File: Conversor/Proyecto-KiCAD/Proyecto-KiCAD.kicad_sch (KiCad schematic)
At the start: 50 parts

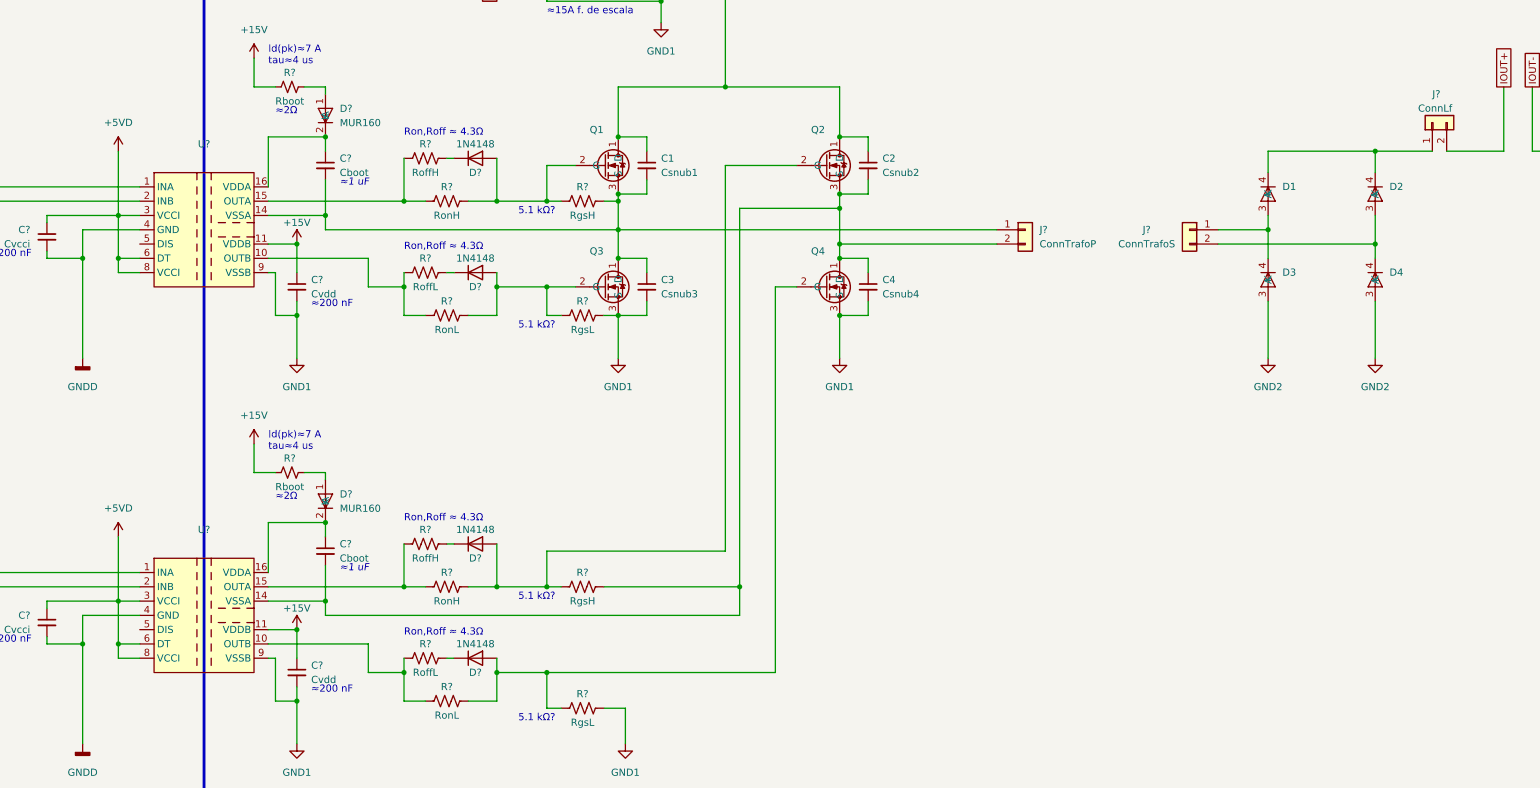
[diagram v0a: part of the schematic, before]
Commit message: Completar las fuentes aisladas del lado digital
- Falta hacer las fuentes del lado de potencia (sin las TRACO).
  - Se tiene que tomar la entrada de 12V-18V y pasarla por un regulador de 15V.
  - Despues esa salida de 15V se pasa por un regulador que la baje a 5V.
- Agregadas datasheets y notas:
  - Datasheets de regulador LM1117 para pasar de 5V a 3.3V para alimentar el DSP.
  - Notas de aplicacion de la fuente TRACO y explicaciones de corrientes sink y source.
- Hay que ver las cosas que me tiene que pasar Jorge de la alimentacion del DSP.
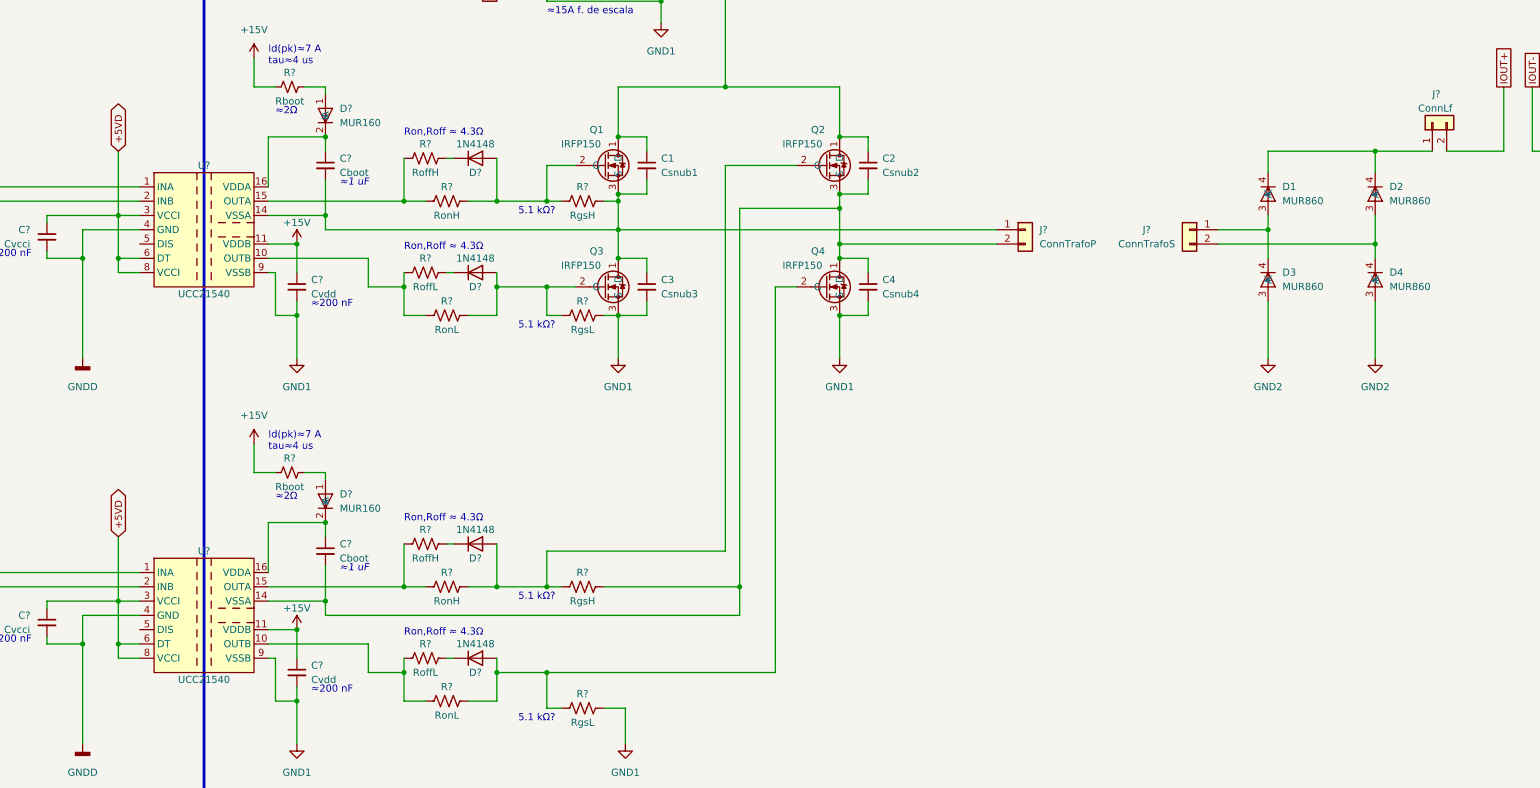
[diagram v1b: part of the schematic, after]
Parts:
- D1, D2, D3, D4: value (none) -> MUR860; footprint (none) -> Package_TO_SOT_THT:TO-220F-2_Vertical
- Q1, Q2, Q3, Q4: value (none) -> IRFP150; footprint (none) -> Package_TO_SOT_THT:TO-247-3_Vertical
- U? (x2): value (none) -> UCC21540; footprint (none) -> Package_SO:SOIC-16W_7.5x10.3mm_P1.27mm

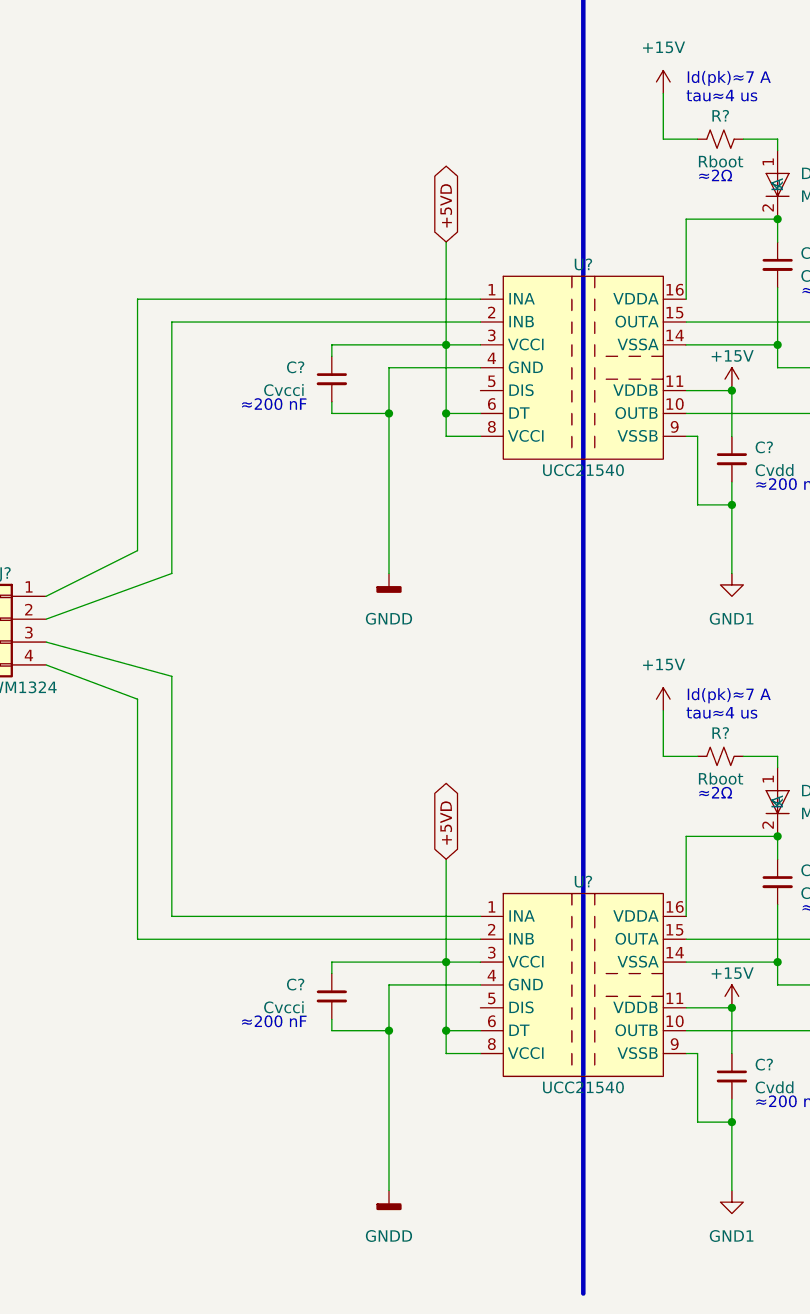
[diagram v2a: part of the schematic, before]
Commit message: Modificar las fuentes de alimentacion
- Falta la fuente regulada de 15V para Vdd de los drivers (Sale a partir de alimentacion de 24V?)
- El DSP se alimenta por +5V a traves de la placa de prueba
- 3.3V para la proteccion a la salida del AO del ACS709
- Agregada datasheet del regulador MC7805 de 12-18V a 5VP
- Uso el pin de dead-time (DT) de los drivers para evitar corto en una pata del
  puente de MOSFETs (200ns de dead-time)
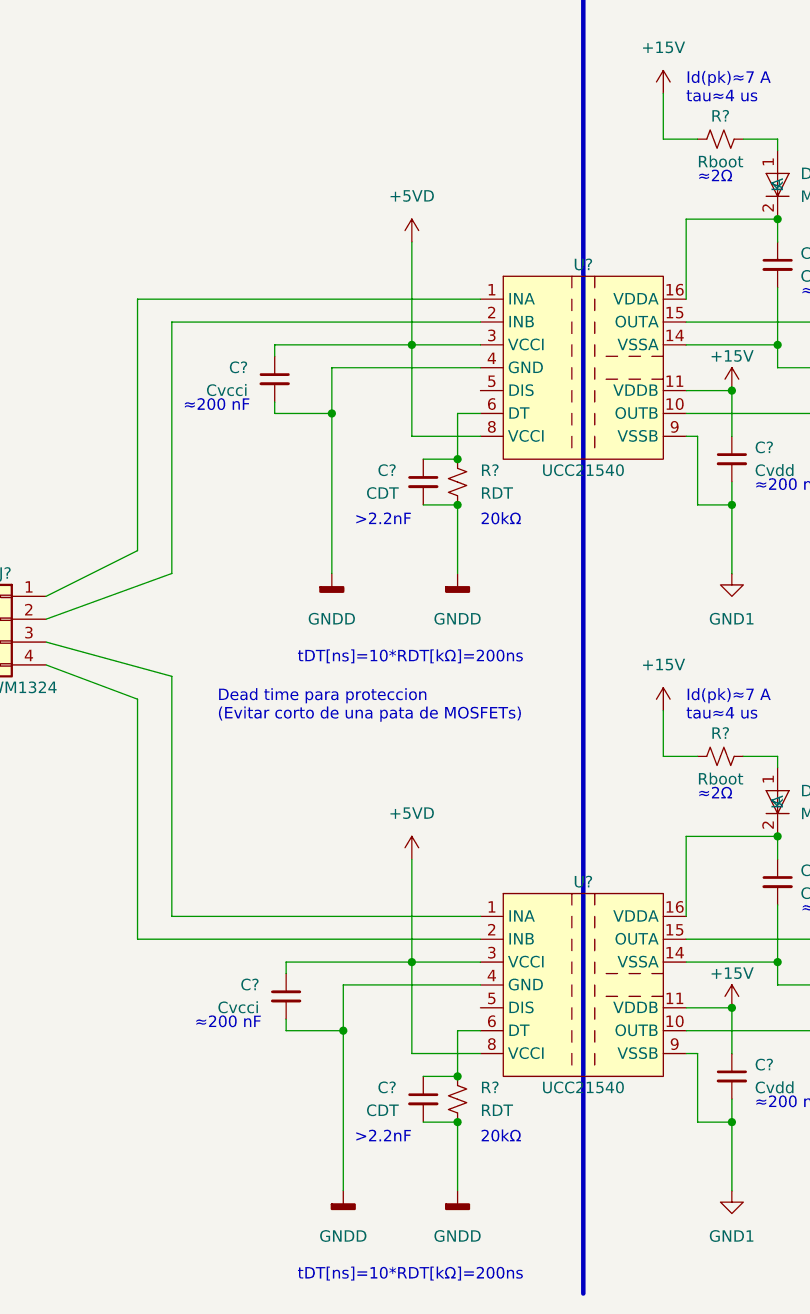
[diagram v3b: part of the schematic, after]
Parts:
- added C? (x2): CDT, symbol Device:C_Small
- added R? (x2): RDT, symbol Device:R_Small_US
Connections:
- net +5VD: no longer U?.6 (DT), U?.6 (DT)
- net GNDD: now also C?.2, C?.2, R?.2, R?.2
- new net: C?.1, R?.1, U?.6 (DT) (x2)
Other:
- note added: "20kΩ"
- note added: ">2.2nF"
- note added: "Dead time para proteccion (Evitar corto de una pata de MOSFETs)"
- note added: "tDT[ns]=10*RDT[kΩ]=200ns"
- moved on the sheet: C?

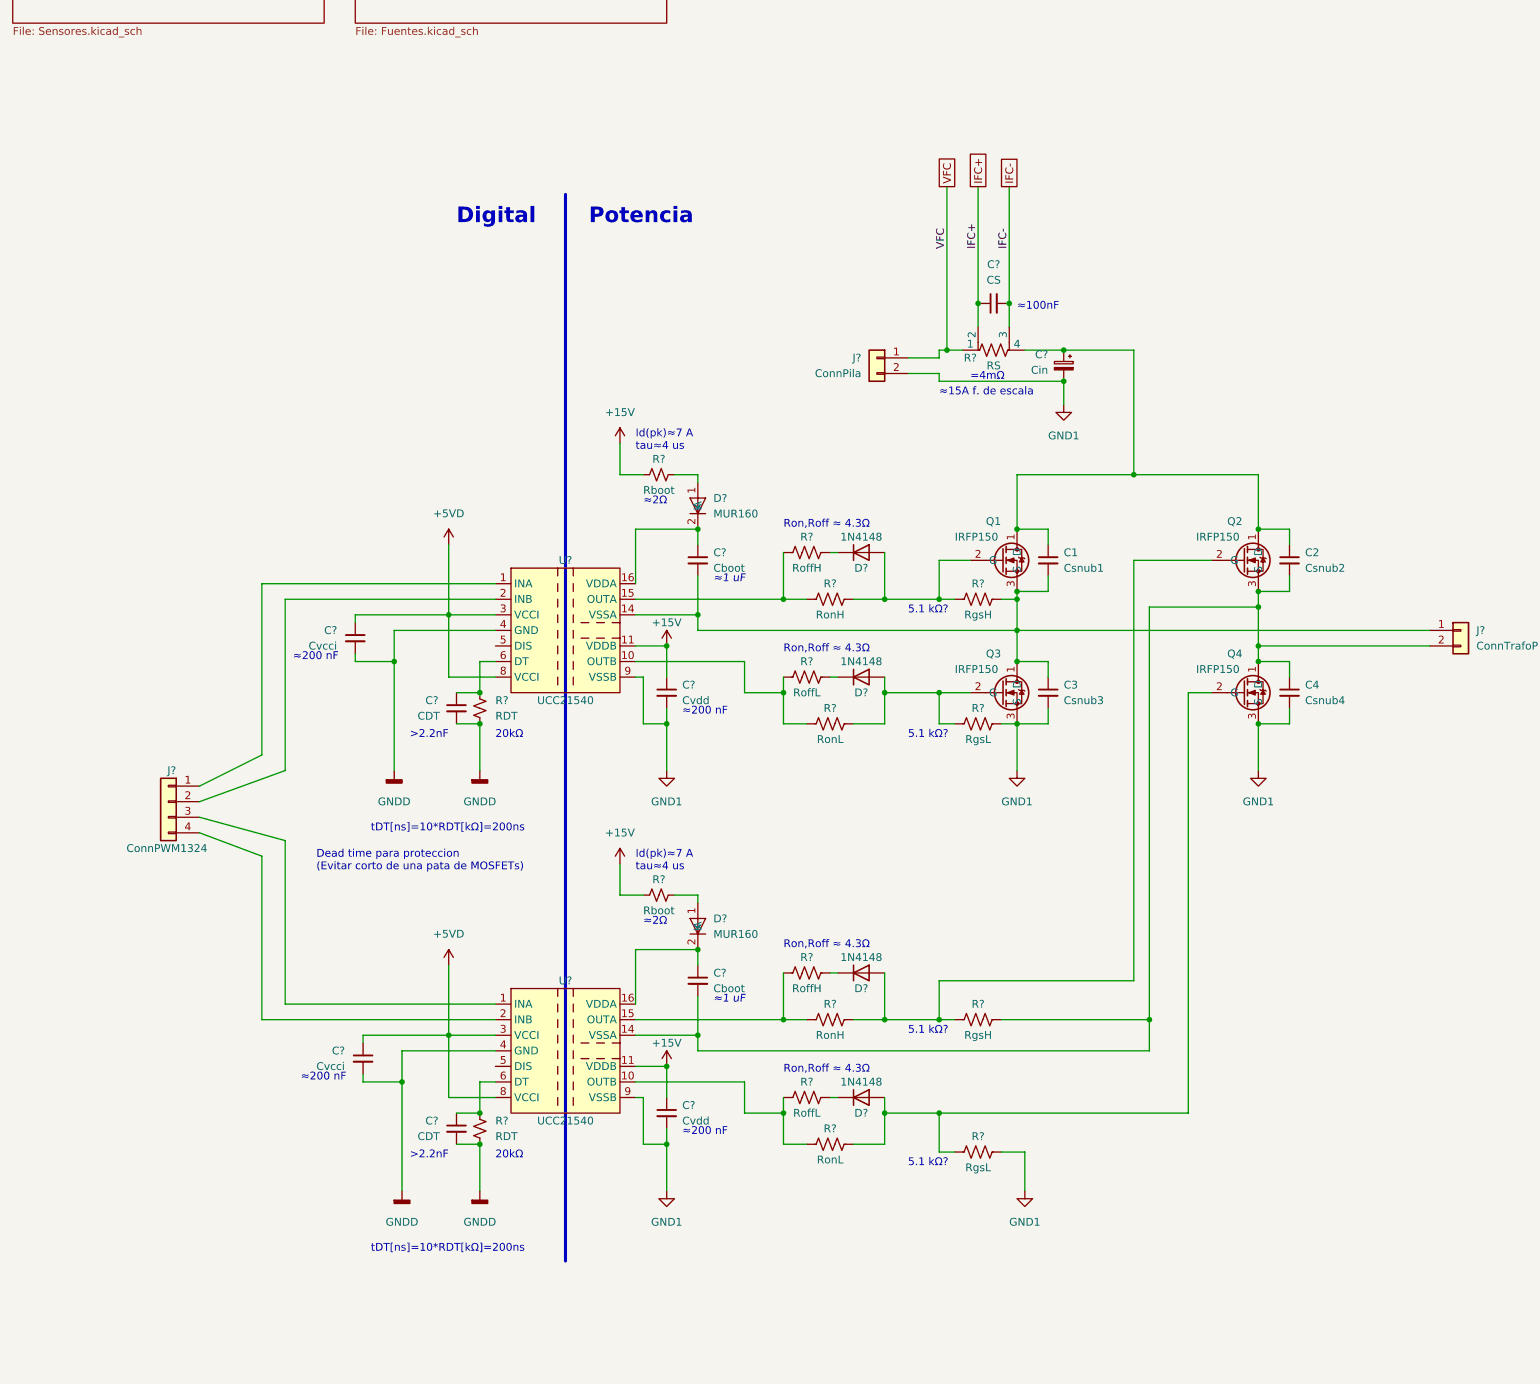
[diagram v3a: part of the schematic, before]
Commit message: Cambiar	drivers	por ADuM4221 de	Analog y completar alimentacion
- UCC21540 y UCC27200 sin stock:
	- Reemplazado por el ADuM4221/ADuM4221-1 de Analog, que es muy similar
	- Alternativa el LTC7061, que tiene DT pero no es aislado
- Aisladores sin stock, falta buscar un reemplazo
- Agregadas las hojas de datos
- LM5056A con poco stock (Hay que comprar muy pronto)
- Completada la lista de componentes con todos los integrados/diodos/transistores
- Agregada nota de aplicacion sobre peak source y sink current
- Agregadas bibliotecas del ADuM4421 y LM5056A bajadas de las paginas de Analog y TI respectivamente
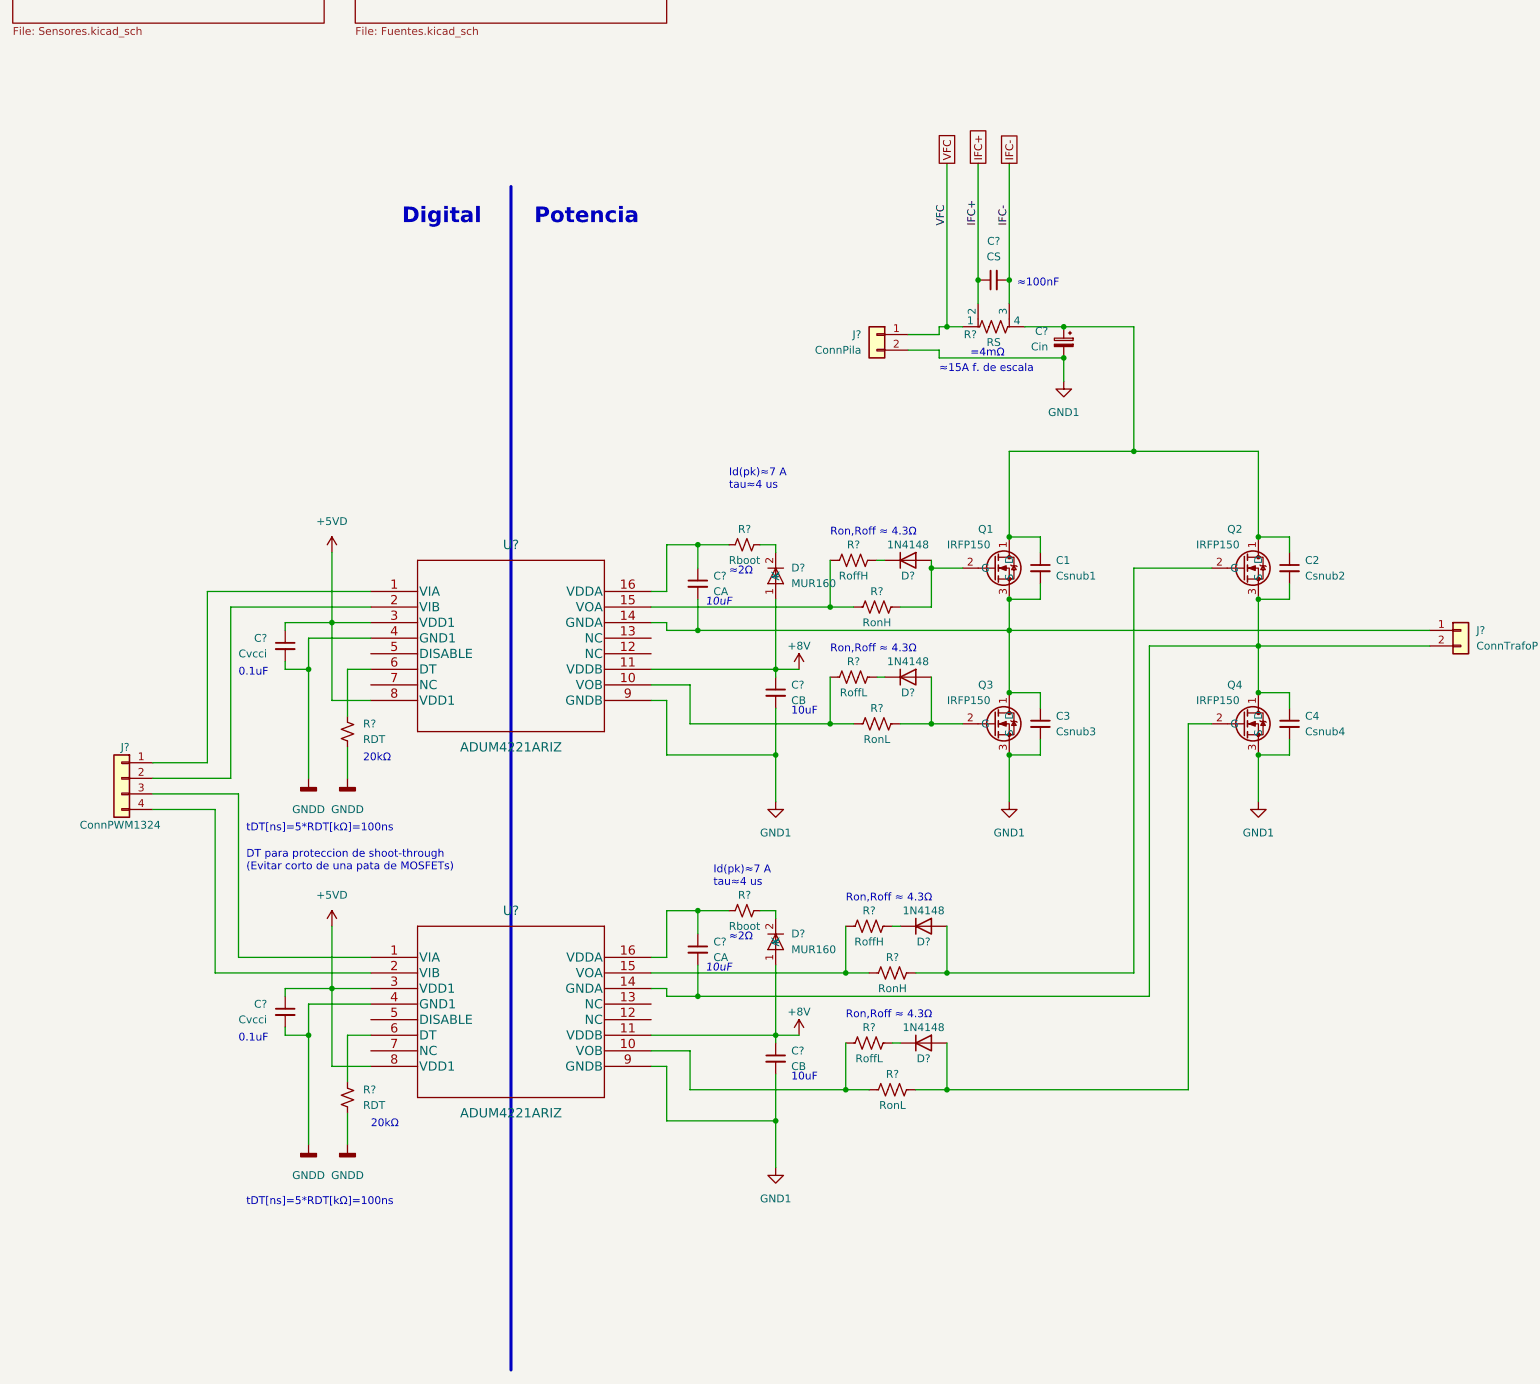
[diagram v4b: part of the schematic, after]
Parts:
- removed C? (x2): CDT, symbol Device:C_Small
- removed C?: Cboot, symbol Device:C_Small
- removed C?: Cvdd, symbol Device:C_Small
- removed D?: MUR160, symbol Componentes proyecto:MUR160
- removed R? (x2): RgsL, symbol Device:R_US
- removed R?: Rboot, symbol Device:R_Small_US
- removed R? (x2): RgsH, symbol Device:R_US
- removed U? (x2): UCC21540, Package_SO:SOIC-16W_7.5x10.3mm_P1.27mm, symbol Componentes proyecto:UCC21540
- added C?: CB, symbol Device:C_Small
- added C?: CA, symbol Device:C_Small
- added D?: MUR160, symbol Componentes proyecto:MUR160
- added R?: Rboot, symbol Device:R_Small_US
- added U? (x2): ADUM4221ARIZ, RI-16-2_Creepage_ADI, symbol 2022-05-17_16-55-27:ADUM4221ARIZ
- C?: value Cvdd -> CB
- C?: value Cboot -> CA
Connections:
- net +5VD: now also U?.3 (VDD1), U?.3 (VDD1), U?.8 (VDD1), U?.8 (VDD1)
- net GND1: now also C?.2, U?.9 (GNDB), U?.9 (GNDB)
- net GNDD: now also U?.4 (GND1), U?.4 (GND1)
- net at R?.1, R?.1: now also U?.10 (VOB) (x2)
- net at R?.1, R?.1: now also U?.15 (VOA) (x2)
- net at C2.2, C4.1, J?.2 (Pin_2)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: now also C?.2, U?.14 (GNDA)
- net at R?.2: now also D?.2 (K); no longer D?.1 (A)
- net at R?.1: now also U?.6 (DT) (x2)
- net at C1.2, C3.1, C?.2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: now also U?.14 (GNDA)
- net at J?.3 (Pin_3): now also U?.1 (VIA)
- net at J?.4 (Pin_4): now also U?.2 (VIB)
- net at C?.1: now also R?.1, U?.16 (VDDA); no longer D?.2 (K)
- net at J?.1 (Pin_1): now also U?.1 (VIA)
- net at J?.2 (Pin_2): now also U?.2 (VIB)
- net +15V renamed +8V
- net +8V: now also D?.1 (A), C?.1, D?.1 (A), U?.11 (VDDB), U?.11 (VDDB); no longer R?.1
- new net: D?.2 (K), R?.2
- new net: C?.1, R?.1, U?.16 (VDDA)
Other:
- note added: "0.1uF"
- note added: "10uF"
- note added: "DT para proteccion de shoot-through (Evitar corto de una pata de MOSFETs)"
- note added: "tDT[ns]=5*RDT[kΩ]=100ns"
- note removed: "5.1 kΩ?"
- note removed: ">2.2nF"
- note removed: "Dead time para proteccion (Evitar corto de una pata de MOSFETs)"
- note removed: "tDT[ns]=10*RDT[kΩ]=200ns"
- note removed: "≈1 uF"
- note removed: "≈200 nF"
- moved on the sheet: C1, C2, C3, C4, C?, D?, J?, Q1, Q2, Q3, Q4, R?
